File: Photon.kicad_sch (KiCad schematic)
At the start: 44 parts, among them J1 USB_C_Receptacle_USB2.0_14P, J101 Conn_01x05_Socket, Q1 IRLML6402, Q2 IRLML6402, SW1 TS-1088-AR02016, U101 PY32F002AL15S6TU, U2 RT8059GJ5, U3 TP4056, U4 BCR421UW6-7, U5 DW01A, U6 FS8205A, U7 BCR421UW6-7

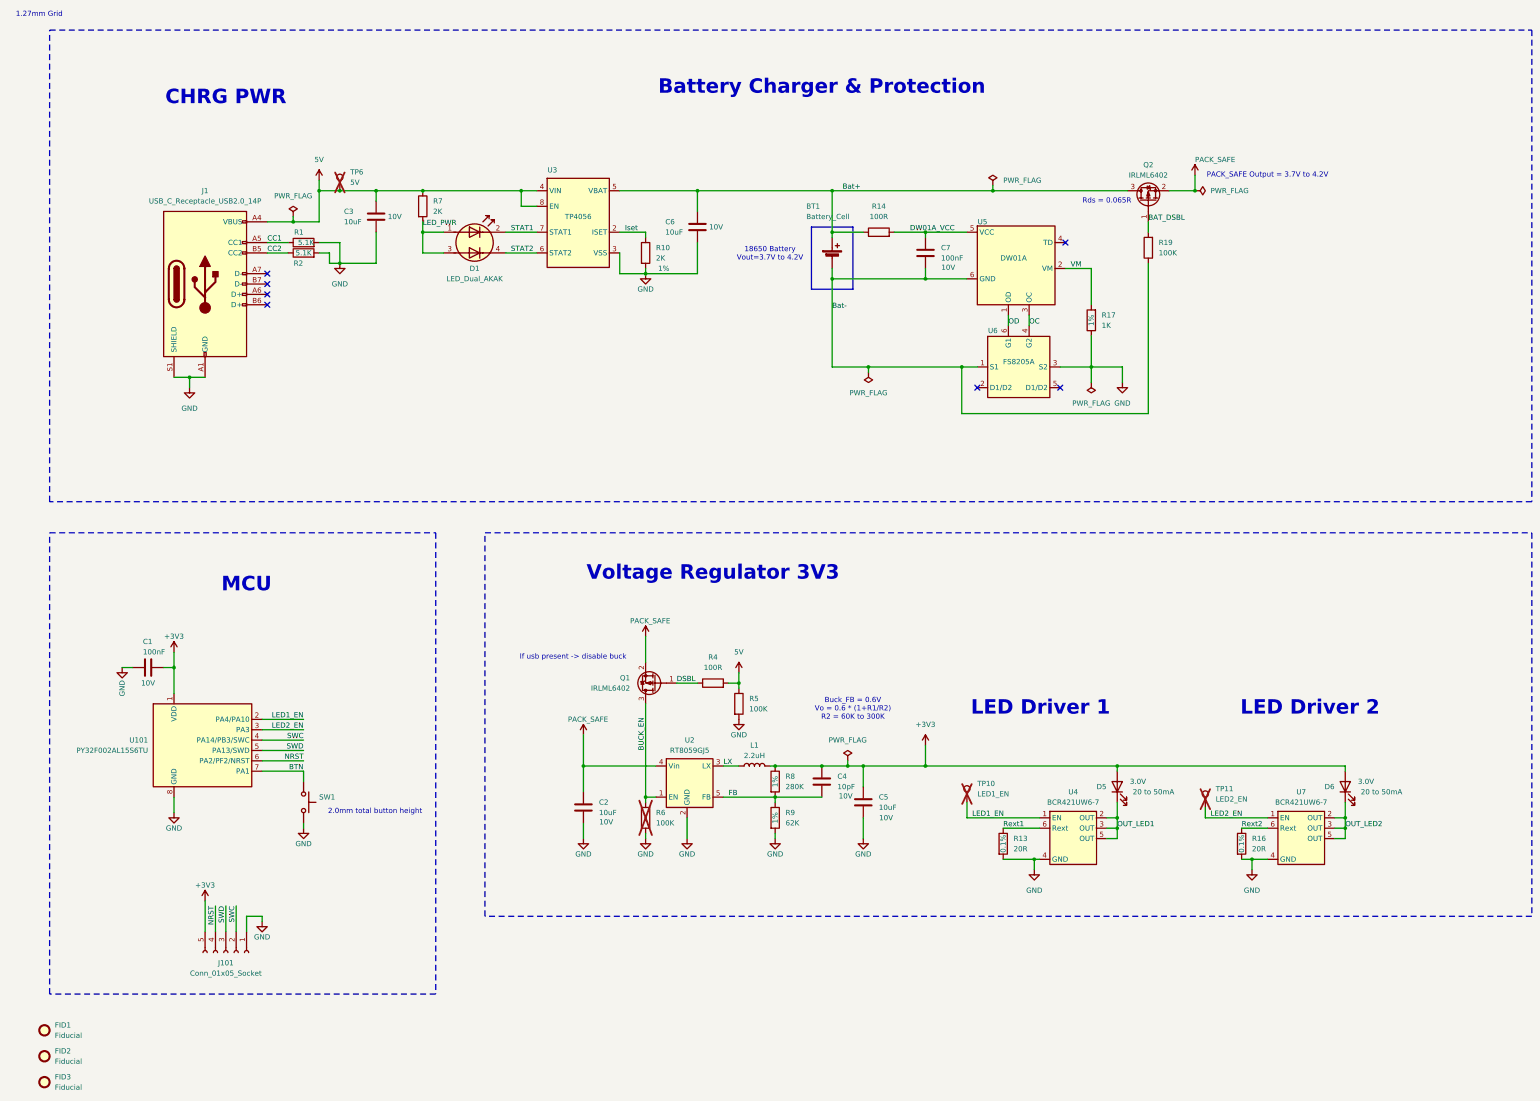
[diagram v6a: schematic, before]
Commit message: improvements
- added pull down to buck (previously there and was removed)
- Simplified PCB by rotating components to reduce vias
- updated value fields and annotated schematic
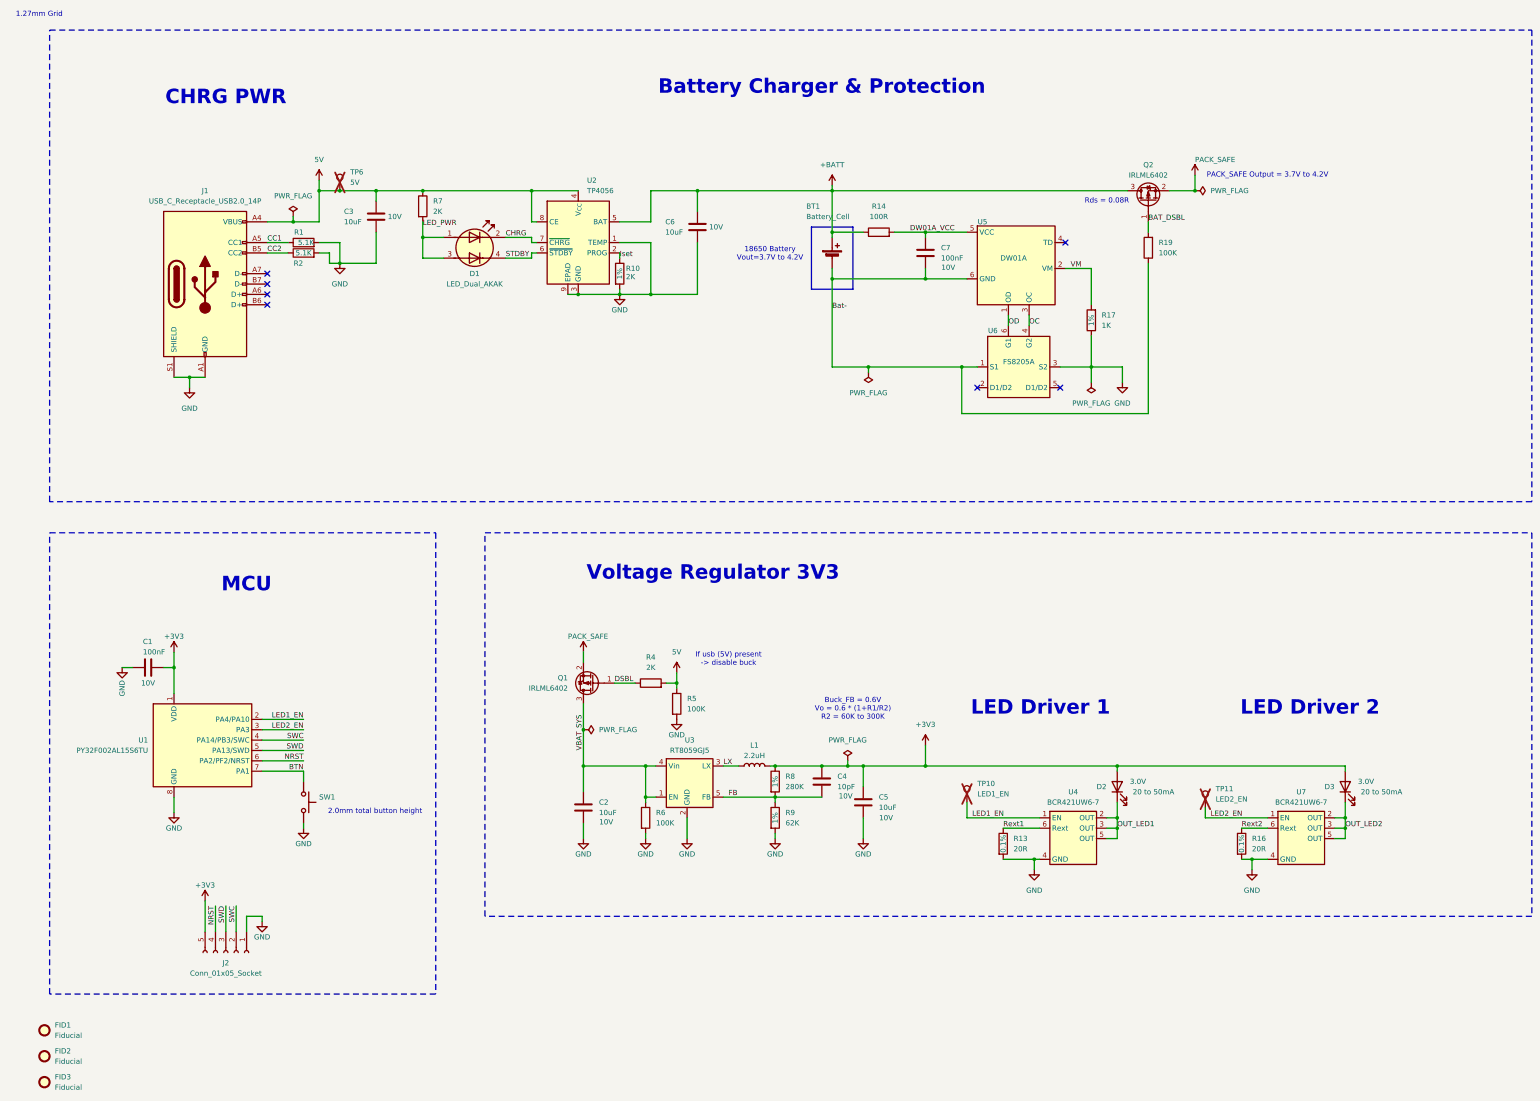
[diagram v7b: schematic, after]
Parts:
- removed U3: TP4056, Package_SO:SOIC-8-1EP_3.9x4.9mm_P1.27mm_EP2.29x3mm, symbol Photon:TP4056
- added U2: TP4056, Package_SO:SOIC-8-1EP_3.9x4.9mm_P1.27mm_EP2.41x3.3mm, symbol Battery_Management:TP4056-42-ESOP8
- R4: value 100R -> 2K
- R6: now fitted
- renumbered D5 to D2, D6 to D3, J101 to J2, U101 to U1, U2 to U3
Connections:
- net 5V: now also U2.4 (V_{CC}), U2.8 (CE)
- net GND: now also U2.1 (TEMP), U2.3 (GND), U2.9 (EPAD)
- net Iset: now also U2.2 (PROG)
- net PACK_SAFE: no longer C2.2, U3.4 (Vin)
- net BUCK_EN renamed VBAT_SYS
- net VBAT_SYS: now also C2.2, U3.4 (Vin)
- net Bat+ renamed +BATT
- net +BATT: now also U2.5 (BAT)
- net STAT1 renamed CHRG
- net CHRG: now also U2.7 (~{CHRG})
- net STAT2 renamed STDBY
- net STDBY: now also U2.6 (~{STDBY})
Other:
- note added: "If usb (5V) present -> disable buck"
- note added: "Rds = 0.08R"
- note removed: "If usb present -> disable buck"
- note removed: "Rds = 0.065R"
- moved on the sheet: D1, Q1, R10, R4, R5

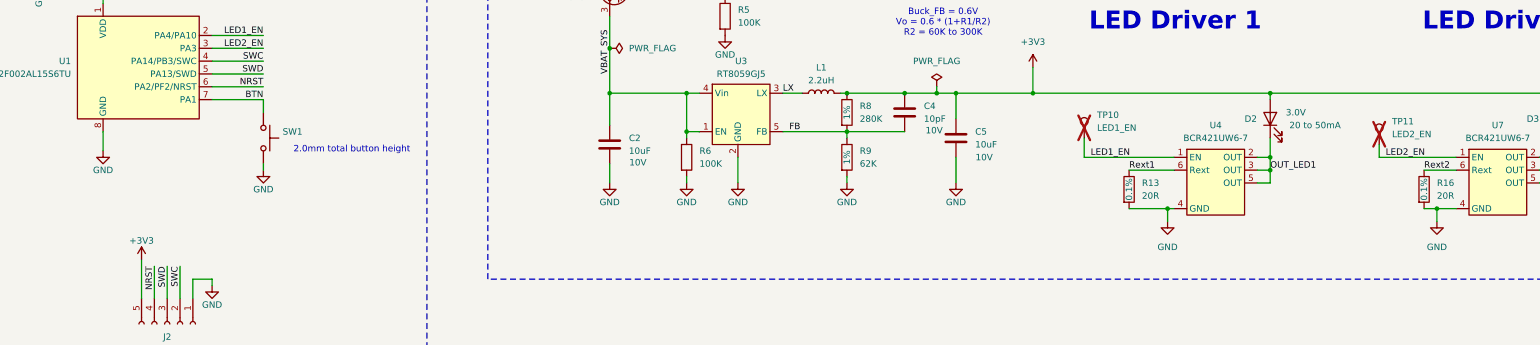
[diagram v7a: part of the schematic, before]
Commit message: added UVLO for the buck
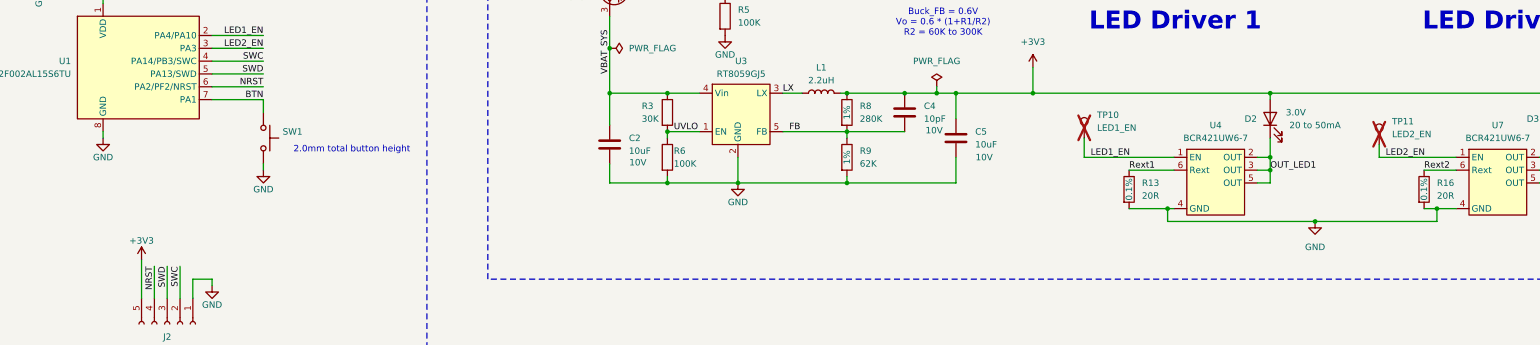
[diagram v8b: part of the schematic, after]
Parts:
- added R3: 30K, Resistor_SMD:R_0603_1608Metric, symbol Device:R
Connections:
- net VBAT_SYS: now also R3.1; no longer R6.1, U3.1 (EN)
- new net UVLO: R3.2, R6.1, U3.1 (EN)
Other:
- moved on the sheet: R6
